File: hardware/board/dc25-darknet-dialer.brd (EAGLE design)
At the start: 101.6 x 101.6 mm, 80 parts, among them SW1 RESET, X1 USB-MICROB

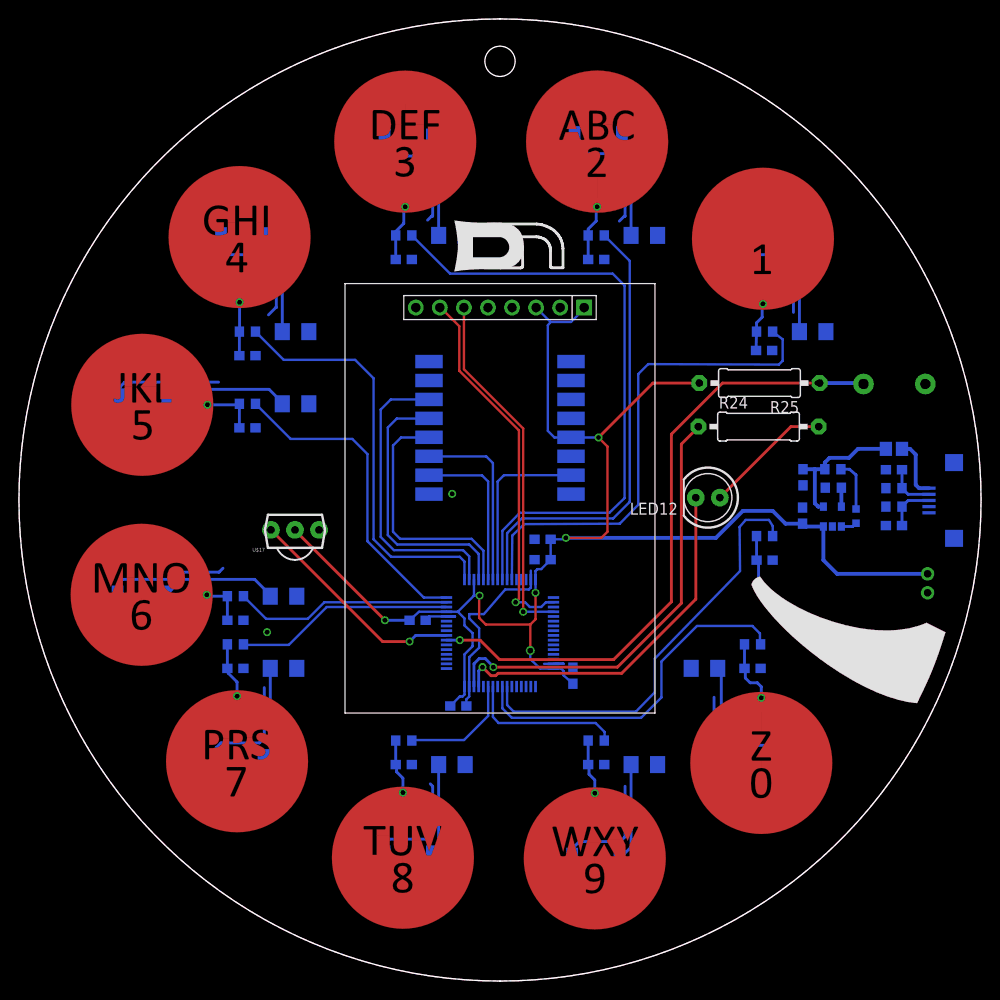
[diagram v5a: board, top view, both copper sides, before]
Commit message: Connected LEDs
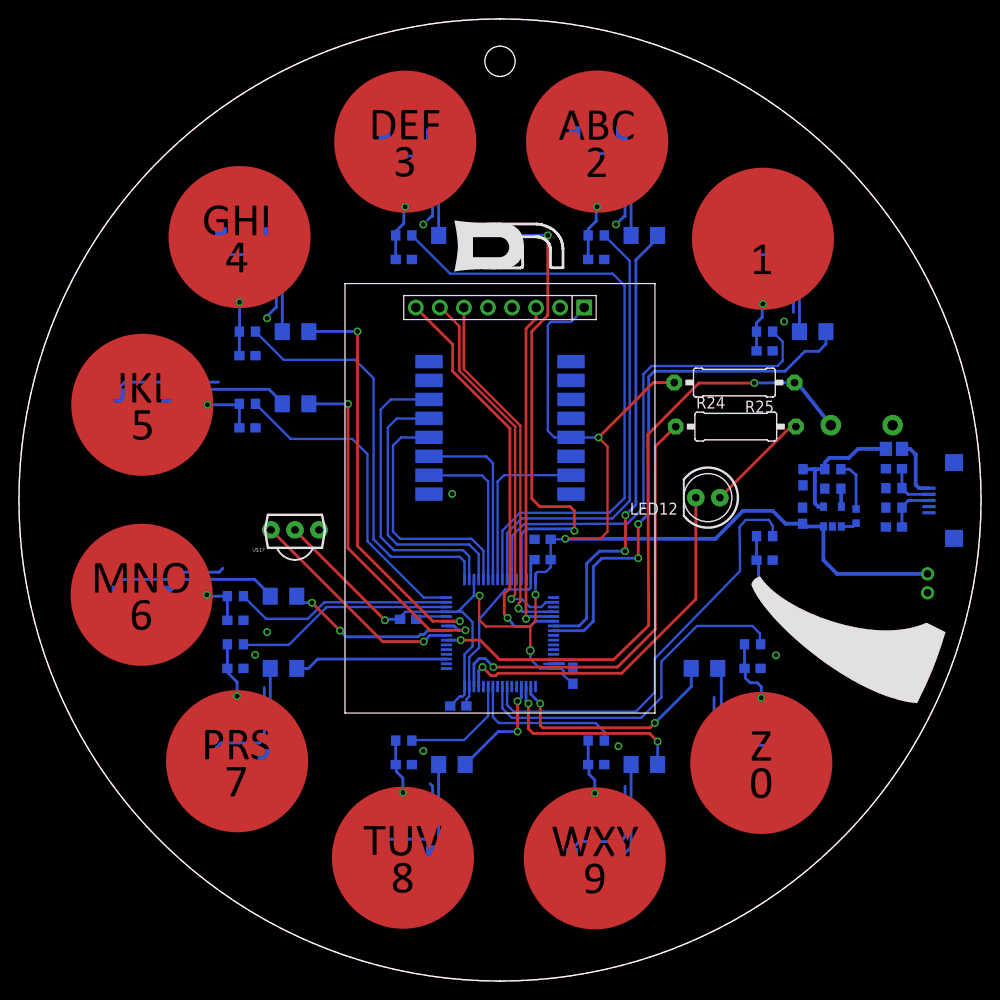
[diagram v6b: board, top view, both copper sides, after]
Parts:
- moved SW1 5.55 mm to (89.0, 58.7)
- moved R25 2.65 mm to (75.5, 63.2)
- moved R24 2.40 mm to (75.7, 58.5)
- moved C15 1.00 mm to (41.1, 38.2)
- moved C19 0.15 mm to (92.4, 48.0)
- moved R22 0.11 mm to (86.0, 52.0)
- moved C20 0.10 mm to (92.4, 54.1)
- moved R27 0.10 mm to (92.4, 50.0)
- moved C1 0.07 mm to (78.7, 66.5)
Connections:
- net N$57 renamed IR_RCV
- removed net N$46 (its old number): U$2.P52
- removed net N$47: U$2.P51
- removed net N$48 (its old number): U$2.P50
- removed net N$50: U$2.P40
- removed net N$51: U$2.P39
- removed net N$52: U$2.P38
- removed net N$53: U$2.P37
- removed net N$54: U$2.P3
- removed net N$58: U$2.P9
- removed net N$59: U$2.P10
- removed net N$60: U$2.P11
- removed net N$61 (its old number): U$2.P29
- removed net N$62: U$12.LED
- new net OLED_CS: U$12.CS, U$2.P37
- new net OLED_LED: U$12.LED, U$2.P38
- net LED1: now also U$2.P40
- net LED10: now also U$2.P50
- net LED2: now also U$2.P39
- net LED3: now also U$2.P29
- net LED4: now also U$2.P11
- net LED5: now also U$2.P10
- net LED6: now also U$2.P9
- net LED7: now also U$2.P3
- net LED8: now also U$2.P52
- net LED9: now also U$2.P51
- net VCC: no longer U$12.CS
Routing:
- net LED1: track 0.00 -> 56.6 mm, vias 0 -> 2
- net LED3: track 0.00 -> 55.1 mm, vias 0 -> 2
- net LED2: track 0.00 -> 49.0 mm, vias 0 -> 2
- net LED4: track 0.00 -> 43.3 mm, vias 0 -> 2
- net OLED_LED: track 0.00 -> 42.8 mm, vias 0 -> 1
- net LED5: track 0.00 -> 37.6 mm, vias 0 -> 2
- net OLED_CS: track 0.00 -> 36.3 mm, vias 0 -> 1
- net LED10: track 0.00 -> 24.3 mm, vias 0 -> 2
- net LED9: track 0.00 -> 21.2 mm, vias 0 -> 2
- net LED6: track 0.00 -> 17.9 mm, vias 0 -> 2
- net LED7: track 0.00 -> 16.2 mm
- net LED8: track 0.00 -> 11.9 mm, vias 0 -> 2
- net VCC: track 163.2 -> 159.4 mm
- net N$23: track 13.5 -> 11.1 mm
- net GND: track 151.1 -> 149.8 mm, vias 2 -> 10
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
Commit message: Added resonator
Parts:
- added Y1: RESONATORSMD, SparkFun:RESONATOR-SMD
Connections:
- net GND: now also Y1.2
- net RCC_OSC_IN: now also Y1.1
- net RCC_OSC_OUT: now also Y1.3
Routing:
- net RCC_OSC_IN: track 0.00 -> 5.28 mm
- net LED7: track 16.2 -> 20.9 mm
- net RCC_OSC_OUT: track 0.00 -> 3.70 mm
